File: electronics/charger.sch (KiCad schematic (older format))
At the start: 17 parts, among them U1 CS5080E

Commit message: Slightly change electronics
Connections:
- net labels added: BATT, VBUS
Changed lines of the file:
@@
 	0    -1   -1   0
 $EndComp
+Text Label 8600 4650 0    50   ~ 0
+BATT
+Text Label 2300 3050 0    50   ~ 0
+VBUS
 $EndSCHEMATC

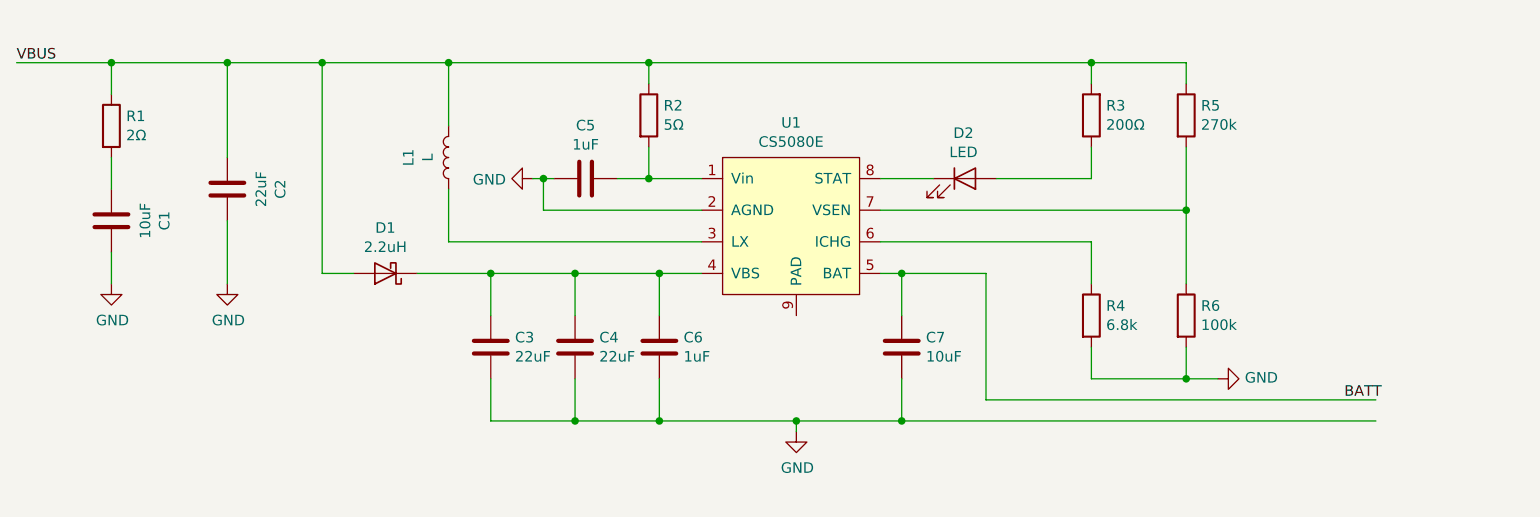
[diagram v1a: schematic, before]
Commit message: Change to electronics, and adding pi dimensions into documents
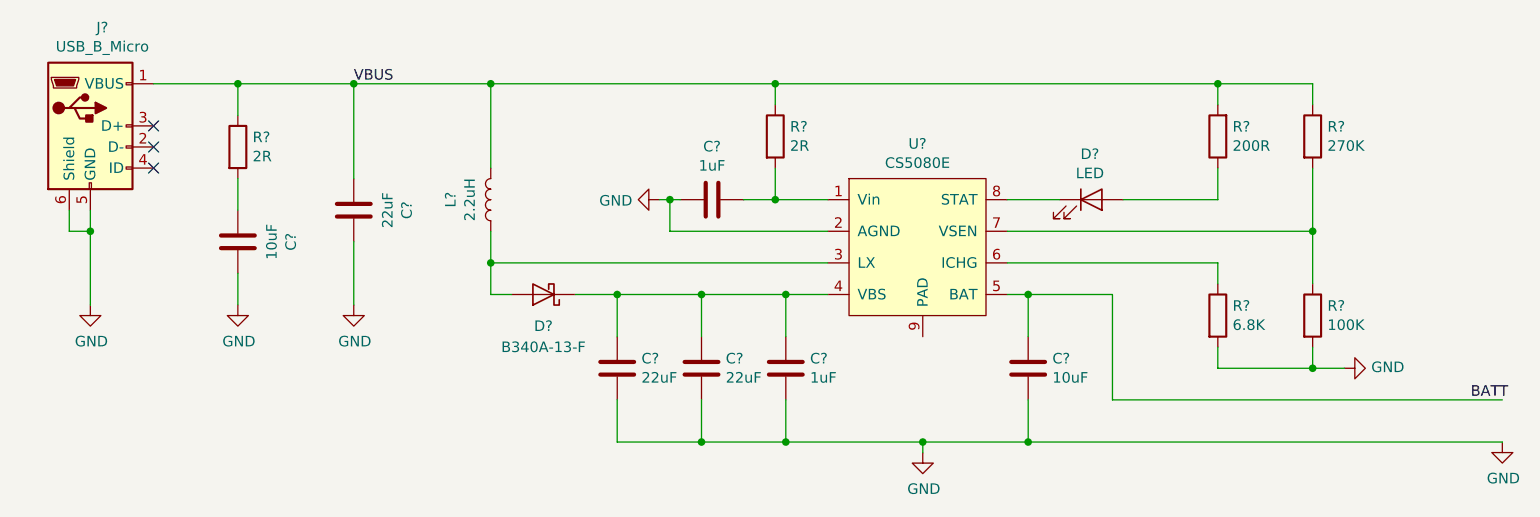
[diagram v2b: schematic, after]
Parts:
- added J?: USB_B_Micro, Connector_USB:USB_Micro-B_GCT_USB3076-30-A, symbol Connector:USB_B_Micro
- C?: renamed from C5; footprint (none) -> Capacitor_SMD:C_0805_2012Metric
- C?: renamed from C2; footprint (none) -> Capacitor_SMD:C_1206_3216Metric
- C?: renamed from C1; footprint (none) -> Capacitor_SMD:C_1206_3216Metric
- C?: renamed from C6; footprint (none) -> Capacitor_SMD:C_0805_2012Metric
- C?: renamed from C4; footprint (none) -> Capacitor_SMD:C_1206_3216Metric
- C?: renamed from C3; footprint 22uF -> Capacitor_SMD:C_1206_3216Metric
- C?: renamed from C7; footprint (none) -> Capacitor_SMD:C_1206_3216Metric
- D?: renamed from D1; value 2.2uH -> B340A-13-F; footprint (none) -> Diode_SMD:D_SMA
- D?: renamed from D2; footprint (none) -> LED_SMD:LED_0805_2012Metric
- L?: renamed from L1; value L -> 2.2uH; footprint (none) -> Inductor_SMD:L_12x12mm_H6mm
- R?: renamed from R2; value 5Ω -> 2R; footprint (none) -> Resistor_SMD:R_0805_2012Metric
- R?: renamed from R1; value 2Ω -> 2R; footprint (none) -> Resistor_SMD:R_0805_2012Metric
- R?: renamed from R3; value 200Ω -> 200R; footprint (none) -> Resistor_SMD:R_0805_2012Metric
- R?: renamed from R5; value 270k -> 270K; footprint (none) -> Resistor_SMD:R_0805_2012Metric
- R?: renamed from R6; value 100k -> 100K; footprint (none) -> Resistor_SMD:R_0805_2012Metric
- R?: renamed from R4; value 6.8k -> 6.8K; footprint (none) -> Resistor_SMD:R_0805_2012Metric
- renumbered U1 to U?
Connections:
- wire segments 61 -> 64
- no-connect marks 0 -> 3
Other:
- moved on the sheet: C?, D?, L?, R?, U?

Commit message: Preview SCH is done, but not fully finished.
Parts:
- removed J?: USB_B_Micro, Connector_USB:USB_Micro-B_GCT_USB3076-30-A, symbol Connector:USB_B_Micro
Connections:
- no-connect marks 3 -> 0
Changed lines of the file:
@@
 $Descr A4 11693 8268
 encoding utf-8
-Sheet 3 4
-Title "Langpie"
+Sheet 4 4
+Title ""
 Date "2020-04-08"
 Rev "v1.0"
-Comp "Langpie"
-Comment1 "github.com/langpie/langpie.git"
+Comp ""
+Comment1 ""
 Comment2 ""
 Comment3 ""
@@
 	7000 4150 7100 4150
 $Comp
-L power:GND #PWR?
+L power:GND #PWR0110
 U 1 1 5E8CB6D9
 P 6600 4900
-F 0 "#PWR?" H 6600 4650 50  0001 C CNN
+F 0 "#PWR0110" H 6600 4650 50  0001 C CNN
 F 1 "GND" H 6605 4727 50  0000 C CNN
 F 2 "" H 6600 4900 50  0001 C CNN
@@
 $EndComp
 $Comp
-L power:GND #PWR?
+L power:GND #PWR0111
 U 1 1 5E8CBEAD
 P 3350 4200
-F 0 "#PWR?" H 3350 3950 50  0001 C CNN
+F 0 "#PWR0111" H 3350 3950 50  0001 C CNN
 F 1 "GND" H 3355 4027 50  0000 C CNN
 F 2 "" H 3350 4200 50  0001 C CNN
@@
 $EndComp
 $Comp
-L power:GND #PWR?
+L power:GND #PWR0112
 U 1 1 5E8CBEFE
 P 3900 4200
-F 0 "#PWR?" H 3900 3950 50  0001 C CNN
+F 0 "#PWR0112" H 3900 3950 50  0001 C CNN
 F 1 "GND" H 3905 4027 50  0000 C CNN
 F 2 "" H 3900 4200 50  0001 C CNN
@@
 $EndComp
 $Comp
-L power:GND #PWR?
+L power:GND #PWR0113
 U 1 1 5E8DC216
 P 5350 3700
-F 0 "#PWR?" H 5350 3450 50  0001 C CNN
+F 0 "#PWR0113" H 5350 3450 50  0001 C CNN
 F 1 "GND" V 5355 3572 50  0000 R CNN
 F 2 "" H 5350 3700 50  0001 C CNN
@@
 Wire Wire Line
 	3350 3300 3350 3150
-Connection ~ 3350 3150
 Connection ~ 3900 3150
 Wire Wire Line
@@
 	7100 4650 7100 4850
 Wire Wire Line
-	7100 4850 9350 4850
+	7100 4850 9150 4850
 Connection ~ 7100 4850
 Wire Wire Line
-	7500 4650 9350 4650
+	7500 4650 9150 4650
 Wire Wire Line
 	7500 4150 7500 4650
@@
 Connection ~ 8450 4500
 $Comp
-L power:GND #PWR?
+L power:GND #PWR0114
 U 1 1 5E980AC4
 P 8600 4500
-F 0 "#PWR?" H 8600 4250 50  0001 C CNN
+F 0 "#PWR0114" H 8600 4250 50  0001 C CNN
 F 1 "GND" V 8605 4372 50  0000 R CNN
 F 2 "" H 8600 4500 50  0001 C CNN
@@
 	0    -1   -1   0
 $EndComp
-Text Label 9200 4650 0    50   ~ 0
-BATT
-Text Label 3900 3150 0    50   ~ 0
-VBUS
 Wire Wire Line
 	3900 3150 4550 3150
@@
 Wire Wire Line
 	4550 3150 5900 3150
-$Comp
-L power:GND #PWR?
-U 1 1 5E964892
-P 9350 4850
-AR Path="/5E90B2B2/5E964892" Ref="#PWR?"  Part="1"
-AR Path="/5E915994/5E964892" Ref="#PWR?"  Part="1"
-F 0 "#PWR?" H 9350 4600 50  0001 C CNN
-F 1 "GND" H 9355 4677 50  0000 C CNN
-F 2 "" H 9350 4850 50  0001 C CNN
-F 3 "" H 9350 4850 50  0001 C CNN
-	1    9350 4850
-	1    0    0    -1
-$EndComp
-$Comp
-L Connector:USB_B_Micro J?
-U 1 1 5E96F345
-P 2650 3350
-F 0 "J?" H 2707 3817 50  0000 C CNN
-F 1 "USB_B_Micro" H 2707 3726 50  0000 C CNN
-F 2 "Connector_USB:USB_Micro-B_GCT_USB3076-30-A" H 2800 3300 50  0001 C CNN
-F 3 "~" H 2800 3300 50  0001 C CNN
-F 4 "https://item.szlcsc.com/10961.html" H 2650 3350 50  0001 C CNN "Seller"
-	1    2650 3350
-	1    0    0    -1
-$EndComp
-NoConn ~ 2950 3350
-NoConn ~ 2950 3450
-NoConn ~ 2950 3550
-Wire Wire Line
-	2950 3150 3350 3150
-$Comp
-L power:GND #PWR?
-U 1 1 5E979834
-P 2650 4200
-F 0 "#PWR?" H 2650 3950 50  0001 C CNN
-F 1 "GND" H 2655 4027 50  0000 C CNN
-F 2 "" H 2650 4200 50  0001 C CNN
-F 3 "" H 2650 4200 50  0001 C CNN
-	1    2650 4200
-	1    0    0    -1
-$EndComp
-Wire Wire Line
-	2550 3750 2550 3850
-Wire Wire Line
-	2550 3850 2650 3850
-Wire Wire Line
-	2650 3850 2650 3750
-Wire Wire Line
-	2650 3850 2650 4200
-Connection ~ 2650 3850
+Text HLabel 9150 4650 2    50   Input ~ 0
+BATT
+Text HLabel 2650 3150 0    50   Input ~ 0
+VBUS
+Wire Wire Line
+	3350 3150 2650 3150
+Text HLabel 9150 4850 2    50   Input ~ 0
+GND
 $EndSCHEMATC

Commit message: modified:   ../../electronics/charger.sch 	modified:   ../../electronics/charger.sch-bak 	modified:   ../../electronics/dc_dc.sch 	modified:   ../../electronics/dc_dc.sch-bak 	modified:   ../../electronics/langpie.pro 	modified:   ../../electronics/langpie.sch 	modified:   ../../electronics/langpie.sch-bak 	modified:   ../../electronics/motor_driver_rpi_pi.sch 	modified:   ../../electronics/motor_driver_rpi_pi.sch-bak 	modified:   ../../electronics/schematic_v1_preview.pdf
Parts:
- gave numbers to parts that had none: 17
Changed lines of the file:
@@
 $EndDescr
 $Comp
-L langpie:CS5080E U?
+L langpie:CS5080E U3
 U 1 1 5E8CA963
 P 6250 3600
-F 0 "U?" H 6575 3765 50  0000 C CNN
+F 0 "U3" H 6575 3765 50  0000 C CNN
 F 1 "CS5080E" H 6575 3674 50  0000 C CNN
 F 2 "Package_SO:SOIC-8-1EP_3.9x4.9mm_P1.27mm_EP2.29x3mm_ThermalVias" H 6350 3650 50  0001 C CNN
@@
 $EndComp
 $Comp
-L Device:C C?
+L Device:C C13
 U 1 1 5E8CAACB
 P 3900 3750
-F 0 "C?" V 3648 3750 50  0000 C CNN
+F 0 "C13" V 3648 3750 50  0000 C CNN
 F 1 "22uF" V 3739 3750 50  0000 C CNN
 F 2 "Capacitor_SMD:C_1206_3216Metric" H 3938 3600 50  0001 C CNN
@@
 $EndComp
 $Comp
-L Device:C C?
+L Device:C C12
 U 1 1 5E8CAB08
 P 3350 3900
-F 0 "C?" V 3098 3900 50  0000 C CNN
+F 0 "C12" V 3098 3900 50  0000 C CNN
 F 1 "10uF" V 3189 3900 50  0000 C CNN
 F 2 "Capacitor_SMD:C_1206_3216Metric" H 3388 3750 50  0001 C CNN
@@
 $EndComp
 $Comp
-L Device:C C?
+L Device:C C15
 U 1 1 5E8CABF4
 P 5550 4500
-F 0 "C?" H 5435 4454 50  0000 R CNN
+F 0 "C15" H 5435 4454 50  0000 R CNN
 F 1 "22uF" H 5435 4545 50  0000 R CNN
 F 2 "Capacitor_SMD:C_1206_3216Metric" H 5588 4350 50  0001 C CNN
@@
 $EndComp
 $Comp
-L Device:C C?
+L Device:C C14
 U 1 1 5E8CB03F
 P 5150 4500
-F 0 "C?" H 5035 4454 50  0000 R CNN
+F 0 "C14" H 5035 4454 50  0000 R CNN
 F 1 "22uF" H 5035 4545 50  0000 R CNN
 F 2 "Capacitor_SMD:C_1206_3216Metric" H 5188 4350 50  0001 C CNN
@@
 $EndComp
 $Comp
-L Device:C C?
+L Device:C C18
 U 1 1 5E8CB094
 P 7100 4500
-F 0 "C?" H 7215 4546 50  0000 L CNN
+F 0 "C18" H 7215 4546 50  0000 L CNN
 F 1 "10uF" H 7215 4455 50  0000 L CNN
 F 2 "Capacitor_SMD:C_1206_3216Metric" H 7138 4350 50  0001 C CNN
@@
 $EndComp
 $Comp
-L Device:L L?
+L Device:L L2
 U 1 1 5E8CBD76
 P 4550 3700
-F 0 "L?" V 4740 3700 50  0000 C CNN
+F 0 "L2" V 4740 3700 50  0000 C CNN
 F 1 "2.2uH" V 4649 3700 50  0000 C CNN
 F 2 "Inductor_SMD:L_12x12mm_H6mm" H 4550 3700 50  0001 C CNN
@@
 $EndComp
 $Comp
-L Device:R R?
+L Device:R R19
 U 1 1 5E8CC027
 P 3350 3450
-F 0 "R?" H 3420 3496 50  0000 L CNN
+F 0 "R19" H 3420 3496 50  0000 L CNN
 F 1 "2R" H 3420 3405 50  0000 L CNN
 F 2 "Resistor_SMD:R_0805_2012Metric" V 3280 3450 50  0001 C CNN
@@
 $EndComp
 $Comp
-L Device:D_Schottky D?
+L Device:D_Schottky D4
 U 1 1 5E8CCA00
 P 4800 4150
-F 0 "D?" H 4800 4300 50  0000 C CNN
+F 0 "D4" H 4800 4300 50  0000 C CNN
 F 1 "B340A-13-F" H 4800 4400 50  0000 C CNN
 F 2 "Diode_SMD:D_SMA" H 4800 4150 50  0001 C CNN
@@
 $EndComp
 $Comp
-L Device:R R?
+L Device:R R21
 U 1 1 5E8F3FD1
 P 8000 3400
-F 0 "R?" H 7930 3354 50  0000 R CNN
+F 0 "R21" H 7930 3354 50  0000 R CNN
 F 1 "200R" H 7930 3445 50  0000 R CNN
 F 2 "Resistor_SMD:R_0805_2012Metric" V 7930 3400 50  0001 C CNN
@@
 $EndComp
 $Comp
-L Device:LED D?
+L Device:LED D5
 U 1 1 5E8F60D0
 P 7400 3700
-F 0 "D?" H 7393 3916 50  0000 C CNN
+F 0 "D5" H 7393 3916 50  0000 C CNN
 F 1 "LED" H 7393 3825 50  0000 C CNN
 F 2 "LED_SMD:LED_0805_2012Metric" H 7400 3700 50  0001 C CNN
@@
 	8000 3150 8000 3250
 $Comp
-L Device:R R?
+L Device:R R23
 U 1 1 5E8F8B58
 P 8450 3400
-F 0 "R?" H 8520 3446 50  0000 L CNN
+F 0 "R23" H 8520 3446 50  0000 L CNN
 F 1 "270K" H 8520 3355 50  0000 L CNN
 F 2 "Resistor_SMD:R_0805_2012Metric" V 8380 3400 50  0001 C CNN
@@
 $EndComp
 $Comp
-L Device:R R?
+L Device:R R24
 U 1 1 5E8F962D
 P 8450 4250
-F 0 "R?" H 8520 4296 50  0000 L CNN
+F 0 "R24" H 8520 4296 50  0000 L CNN
 F 1 "100K" H 8520 4205 50  0000 L CNN
 F 2 "Resistor_SMD:R_0805_2012Metric" V 8380 4250 50  0001 C CNN
@@
 	8450 3550 8450 3850
 $Comp
-L Device:R R?
+L Device:R R22
 U 1 1 5E8FB4EA
 P 8000 4250
-F 0 "R?" H 8070 4296 50  0000 L CNN
+F 0 "R22" H 8070 4296 50  0000 L CNN
 F 1 "6.8K" H 8070 4205 50  0000 L CNN
 F 2 "Resistor_SMD:R_0805_2012Metric" V 7930 4250 50  0001 C CNN
@@
 	3350 3750 3350 3600
 $Comp
-L Device:C C?
+L Device:C C16
 U 1 1 5E8CAA6D
 P 5600 3700
-F 0 "C?" V 5348 3700 50  0000 C CNN
+F 0 "C16" V 5348 3700 50  0000 C CNN
 F 1 "1uF" V 5439 3700 50  0000 C CNN
 F 2 "Capacitor_SMD:C_0805_2012Metric" H 5638 3550 50  0001 C CNN
@@
 $EndComp
 $Comp
-L Device:C C?
+L Device:C C17
 U 1 1 5E8CAB4B
 P 5950 4500
-F 0 "C?" H 5835 4454 50  0000 R CNN
+F 0 "C17" H 5835 4454 50  0000 R CNN
 F 1 "1uF" H 5835 4545 50  0000 R CNN
 F 2 "Capacitor_SMD:C_0805_2012Metric" H 5988 4350 50  0001 C CNN
@@
 	5750 3700 5900 3700
 $Comp
-L Device:R R?
+L Device:R R20
 U 1 1 5E8CB8B9
 P 5900 3400
-F 0 "R?" H 5970 3446 50  0000 L CNN
+F 0 "R20" H 5970 3446 50  0000 L CNN
 F 1 "2R" H 5970 3355 50  0000 L CNN
 F 2 "Resistor_SMD:R_0805_2012Metric" V 5830 3400 50  0001 C CNN

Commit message: Finish PCB, silightly change to SCH, Gerber generated, V1.0 HW almost done.
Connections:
- net GND: now also U3.9 (PAD)
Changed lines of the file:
@@
 Text HLabel 9150 4850 2    50   Input ~ 0
 GND
+Wire Wire Line
+	6600 4350 6600 4850
 $EndSCHEMATC
